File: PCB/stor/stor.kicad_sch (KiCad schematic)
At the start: 32 parts, among them J1 Conn_01x04_Socket, SW1 TS1603-TZ38HBM, SW2 TS1603-TZ38HBM, U1 STM32H723VGT6, U2 TYPE-C 24P-GTJB 040, U3 USB3300-EZK-TR, U4 TPS62177DQCR, X1 25mhz, X2 32.768k

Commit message: fill out usb phy
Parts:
- added R5: 12k, easyeda2kicad:R0402, symbol easyeda2kicad:RC0402FR-0712KL
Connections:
- net D+: now also U3.7 (DP)
- net D-: now also U3.8 (DM)
- net GND: now also Card1.10 (GND), Card1.11 (GND), Card1.12 (GND), Card1.13 (GND), Card1.6 (VSS), U3.1 (GND), U3.2 (GND), U3.33 (EPAD), R5.1
- net VBUS: now also U3.4 (VBUS)
- net VDD: now also Card1.4 (VDD), U3.16 (VDD3.3), U3.25 (VDD3.3), U3.30 (VDD3.3), U3.6 (VDD3.3)
- net PC0: now reaches U1.15 (PC0)
- net PC0: now also U3.13 (STP)
- net PC2: now reaches U1.17 (PC2_C)
- net PC2: now also U3.12 (DIR)
- net PC3: now reaches U1.18 (PC3_C)
- net PC3: now also U3.11 (NXT)
- net PA3: now reaches U1.25 (PA3)
- net PA3: now also U3.24 (DATA0)
- net PA5: now reaches U1.29 (PA5)
- net PA5: now also U3.14 (CLKOUT)
- net PB0: now reaches U1.34 (PB0)
- net PB0: now also U3.23 (DATA1)
- net PB1: now reaches U1.35 (PB1)
- net PB1: now also U3.22 (DATA2)
- net PB10: now reaches U1.46 (PB10)
- net PB10: now also U3.21 (DATA3)
- net PB11: now reaches U1.47 (PB11)
- net PB11: now also U3.20 (DATA4)
- net PB12: now reaches U1.51 (PB12)
- net PB12: now also U3.19 (DATA5)
- net PB13: now reaches U1.52 (PB13)
- net PB13: now also U3.18 (DATA6)
- net PC8: now reaches U1.65 (PC8)
- net PC8: now also Card1.7 (DAT0(D0))
- net PC9: now reaches U1.66 (PC9)
- net PC9: now also Card1.8 (DAT1(RSV))
- net PC10: now reaches U1.78 (PC10)
- net PC10: now also Card1.1 (DAT2(RSV))
- net PC11: now reaches U1.79 (PC11)
- net PC11: now also Card1.2 (CDDAT3(CS))
- net PD2: now reaches U1.83 (PD2)
- net PD2: now also Card1.3 (CMD(DI))
- net PB5: now reaches U1.91 (PB5)
- net PB5: now also U3.17 (DATA7)
- net at U3.32 (RBIAS): now also R5.2
- net PC12: now reaches Card1.5 (CLK(SCLK))
- no-connect marks 11 -> 14
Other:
- note added: "SD"
- note added: "TODO Card detect pin"
- note added: "TODO put a crystal here"
- note added: "USB PHY"
- note added: "to a GPIO"

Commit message: usb phy
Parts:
- added C18, C20, C22: 4.7uF, easyeda2kicad:C0402, symbol easyeda2kicad:CL05A475KP5NRNC
- added C19, C21, C23: 100nF, easyeda2kicad:C0402, symbol easyeda2kicad:CC0402KRX7R7BB104
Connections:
- net GND: now also C18.1, C19.1, C20.1, C21.1, C22.1, C23.1
- net at U3.15 (VDD1.8): now also C18.2, C19.2
- net at U3.26 (VDD1.8): now also C20.2, C21.2
- net XO: now reaches U3.27 (XO)
- net XI: now reaches U3.28 (XI)
- net at U3.29 (VDDA1.8): now also C22.2, C23.2
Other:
- moved on the sheet: Card1, R5, U3

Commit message: usb phy p much done and dusted
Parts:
- added C24, C25: 33pF, easyeda2kicad:C0402, symbol easyeda2kicad:CL05C330JB5NNNC
- added R6: 1mΩ, easyeda2kicad:R0402, symbol easyeda2kicad:RC0402FR-071ML
- added X3: 24mhz, easyeda2kicad:CRYSTAL-SMD_4P-L3.2-W2.5-BL, symbol easyeda2kicad:SX32Y024000BC1T001
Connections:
- net GND: now also C24.1, C25.1, X3.2 (GND), X3.4 (GND)
- net XI: now also C25.2, R6.2, X3.3
- net XO: now also C24.2, R6.1, X3.1
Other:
- moved on the sheet: C20, C21

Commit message: Update stor.kicad_sch
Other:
- note added: "TODO add esd protection"
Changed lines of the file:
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@@
+		)
+	)
+	(text "TODO add esd protection"
+		(exclude_from_sim no)
+		(at 130.302 224.282 0)
+		(effects
+			(font
+				(size 1.27 1.27)
+			)
 		)
 	)

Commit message: Update stor.kicad_sch
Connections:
- net VDD: now also U3.31 (REG_EN)
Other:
- note removed: "TODO put a crystal here"
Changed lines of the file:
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@@
 		)
 	)
-	(text "TODO put a crystal here"
-		(exclude_from_sim no)
-		(at 229.87 18.034 0)
+	(text "TODO Card detect pin"
+		(exclude_from_sim no)
+		(at 331.216 50.292 0)
 		(effects
 			(font
@@
 		)
 	)
-	(text "TODO Card detect pin"
-		(exclude_from_sim no)
-		(at 331.216 50.292 0)
+	(text "SD"
+		(exclude_from_sim no)
+		(at 275.844 16.51 0)
+		(effects
+			(font
+				(size 2.54 2.54)
+			)
+		)
+	)
+	(text "TODO add esd protection"
+		(exclude_from_sim no)
+		(at 130.302 224.282 0)
 		(effects
 			(font
@@
 		)
 	)
-	(text "SD"
-		(exclude_from_sim no)
-		(at 275.844 16.51 0)
+	(text "USBC"
+		(exclude_from_sim no)
+		(at 121.92 173.99 0)
 		(effects
 			(font
@@
 		)
 	)
-	(text "TODO add esd protection"
-		(exclude_from_sim no)
-		(at 130.302 224.282 0)
+	(text "STM and friends\n"
+		(exclude_from_sim no)
+		(at 32.512 154.178 0)
+		(effects
+			(font
+				(size 2.54 2.54)
+			)
+		)
+	)
+	(text "to a GPIO"
+		(exclude_from_sim no)
+		(at 218.44 113.03 90)
 		(effects
 			(font
@@
 		)
 	)
-	(text "USBC"
-		(exclude_from_sim no)
-		(at 121.92 173.99 0)
+	(text "USB PHY"
+		(exclude_from_sim no)
+		(at 202.692 21.082 0)
 		(effects
 			(font
@@
 		)
 	)
-	(text "STM and friends\n"
-		(exclude_from_sim no)
-		(at 32.512 154.178 0)
+	(text "Power"
+		(exclude_from_sim no)
+		(at 27.178 175.514 0)
 		(effects
 			(font
@@
 		)
 	)
-	(text "to a GPIO"
-		(exclude_from_sim no)
-		(at 218.44 113.03 90)
+	(text "??"
+		(exclude_from_sim no)
+		(at 25.908 45.974 0)
 		(effects
 			(font
@@
 		)
 	)
-	(text "USB PHY"
-		(exclude_from_sim no)
-		(at 202.692 21.082 0)
-		(effects
-			(font
-				(size 2.54 2.54)
-			)
-		)
-	)
-	(text "Power"
-		(exclude_from_sim no)
-		(at 27.178 175.514 0)
-		(effects
-			(font
-				(size 2.54 2.54)
-			)
-		)
-	)
-	(text "??"
-		(exclude_from_sim no)
-		(at 25.908 45.974 0)
+	(text "button, cap"
+		(exclude_from_sim no)
+		(at 27.178 24.892 0)
 		(effects
 			(font
@@
 		)
 	)
-	(text "button, cap"
-		(exclude_from_sim no)
-		(at 27.178 24.892 0)
-		(effects
-			(font
-				(size 1.27 1.27)
-			)
-		)
-	)
 	(junction
 		(at 264.16 54.61)
@@
 		)
 		(stroke
+			(width 0)
+			(type default)
+		)
+	)
+	(wire
+		(pts
+			(xy 220.98 53.34) (xy 223.52 53.34)
+		)
+		(stroke

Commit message: esd protection
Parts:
- added D2: PESD15VL2BT,215, easyeda2kicad:SOT-23-3_L2.9-W1.3-P1.90-LS2.4-BR, symbol easyeda2kicad:PESD15VL2BT,215
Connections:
- net D+: now also D2.2
- net D-: now also D2.1
- net GND: now also D2.3
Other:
- note added: "TODO to a GPIO"
- note removed: "TODO add esd protection"
- note removed: "to a GPIO"
- moved on the sheet: R2, R3, U2

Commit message: schematic is, as far as I know, done!
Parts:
- added C26: 100nF, easyeda2kicad:C0402, symbol easyeda2kicad:CC0402KRX7R7BB104
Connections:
- net VREF is gone; now on net VDD: U1.20 (VREF+)
- net GND: now also C26.1
- net VDD: now also C26.2
- net PD3: now reaches U1.84 (PD3)
- net PD3: now also U3.9 (RESET)
- net PD4: now reaches U1.85 (PD4)
- net PD4: now also Card1.9 (CD)
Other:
- note added: "can be any gpio"
- note removed: "??"
- note removed: "TODO Card detect pin"
- note removed: "TODO to a GPIO"
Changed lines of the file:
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@@
 		)
 	)
-	(text "TODO Card detect pin"
+	(text "can be any gpio\n"
 		(exclude_from_sim no)
-		(at 331.216 50.292 0)
+		(at 330.708 44.704 0)
 		(effects
 			(font
@@
 		)
 	)
-	(text "TODO to a GPIO"
+	(text "can be any gpio"
 		(exclude_from_sim no)
-		(at 218.44 116.078 90)
+		(at 215.646 114.3 90)
 		(effects
 			(font
@@
 		)
 	)
-	(text "??"
-		(exclude_from_sim no)
-		(at 25.908 45.974 0)
-		(effects
-			(font
-				(size 1.27 1.27)
-			)
-		)
-	)
 	(text "button, cap"
 		(exclude_from_sim no)
@@
 	)
 	(junction
+		(at 93.98 116.84)
+		(diameter 0)
+		(color 0 0 0 0)
+	)
+	(junction
 		(at 64.77 48.26)
 		(diameter 0)
@@
 	)
 	(junction
+		(at 93.98 106.68)
+		(diameter 0)
+		(color 0 0 0 0)
+	)
+	(junction
 		(at 63.5 106.68)
 		(diameter 0)
@@
 	(wire
 		(pts
+			(xy 93.98 106.68) (xy 99.06 106.68)
+		)
+		(stroke
+			(width 0)
+			(type default)
+		)
+	)
+	(wire
+		(pts
 			(xy 251.46 19.05) (xy 256.54 19.05)
 		)
@@
 	(wire
 		(pts
+			(xy 109.22 71.12) (xy 116.84 71.12)
+		)
+		(stroke
+			(width 0)
+			(type default)
+		)
+	)
+	(wire
+		(pts
 			(xy 97.79 189.23) (xy 100.33 189.23)
 		)
@@
 	(wire
 		(pts
+			(xy 93.98 116.84) (xy 99.06 116.84)
+		)
+		(stroke
+			(width 0)
+			(type default)
+		)
+	)
+	(wire
+		(pts
 			(xy 80.01 17.78) (xy 80.01 19.05)
 		)
@@
 		)
 	)
+	(label "PD3"
+		(at 157.48 63.5 0)
+		(effects
+			(font
+				(size 1.27 1.27)
+			)
+			(justify left bottom)
+		)
+	)
 	(label "PD2"
 		(at 288.29 50.8 180)
@@
 		)
 	)
+	(label "PD4"
+		(at 157.48 60.96 0)
+		(effects
+			(font
+				(size 1.27 1.27)
+			)
+			(justify left bottom)
+		)
+	)
 	(label "PC0"
 		(at 228.6 106.68 270)
@@
 		)
 	)
+	(label "PD3"
+		(at 218.44 106.68 270)
+		(effects
+			(font
+				(size 1.27 1.27)
+			)
+			(justify right bottom)
+		)
+	)
 	(label "PC15"
 		(at 116.84 43.18 180)
@@
 		)
 	)
+	(label "PD4"
+		(at 326.39 48.26 0)
+		(effects
+			(font
+				(size 1.27 1.27)
+			)
+			(justify left bottom)
+		)
+	)
 	(label "PA5"
 		(at 116.84 93.98 180)
@@
 		)
 	)
+	(label "VDD"
+		(at 109.22 71.12 180)
+		(effects
+			(font
+				(size 1.27 1.27)
+			)
+			(justify right bottom)
+		)
+	)
 	(label "VBUS"
 		(at 147.32 205.74 180)
@@
 		)
 	)
-	(global_label "VREF"
-		(shape input)
-		(at 116.84 71.12 180)
-		(fields_autoplaced yes)
-		(effects
-			(font
-				(size 1.27 1.27)
-			)
-			(justify right)
-		)
-		(property "Intersheetrefs" "${INTERSHEET_REFS}"
-			(at 109.2586 71.12 0)
-			(hide yes)
-			(show_name no)
-			(do_not_autoplace no)
-			(effects
-				(font
-					(size 1.27 1.27)
-				)
-				(justify right)
-			)
-		)
-	)
-	(global_label "VREF"
-		(shape input)
-		(at 29.21 43.18 180)
-		(fields_autoplaced yes)
-		(effects
-			(font
-				(size 1.27 1.27)
-			)
-			(justify right)
-		)
-		(property "Intersheetrefs" "${INTERSHEET_REFS}"
-			(at 21.6286 43.18 0)
-			(hide yes)
-			(show_name no)
-			(do_not_autoplace no)
-			(effects
-				(font
-					(size 1.27 1.27)
-				)
-				(justify right)
-			)
-		)
-	)
 	(symbol
 		(lib_id "easyeda2kicad:RC0402FR-071ML")
@@
 					(unit 1)
 				)
+			)
+		)
+	)
+	(symbol
+		(lib_id "easyeda2kicad:CC0402KRX7R7BB104")
+		(at 99.06 111.76 90)
+		(unit 1)
+		(body_style 1)
+		(exclude_from_sim no)
+		(in_bom yes)
+		(on_board yes)
+		(in_pos_files yes)
+		(dnp no)
+		(fields_autoplaced yes)
+		(property "Reference" "C26"
+			(at 102.87 110.4899 90)
+			(show_name no)
+			(do_not_autoplace no)
+			(effects
+				(font
+					(size 1.27 1.27)
+				)
+				(justify right)
+			)
+		)
+		(property "Value" "100nF"
+			(at 102.87 113.0299 90)
+			(show_name no)
+			(do_not_autoplace no)
+			(effects
+				(font
+					(size 1.27 1.27)
+				)
+				(justify right)
+			)
+		)
+		(property "Footprint" "easyeda2kicad:C0402"
+			(at 106.68 111.76 0)
+			(hide yes)
+			(show_name no)
+			(do_not_autoplace no)
+			(effects
+				(font
+					(size 1.27 1.27)
+				)
+			)
+		)
+		(property "Datasheet" "https://lcsc.com/product-detail/Multilayer-Ceramic-Capacitors-MLCC-SMD-SMT_100nF-104-10-16V_C60474.html"
+			(at 109.22 111.76 0)
+			(hide yes)
+			(show_name no)
+			(do_not_autoplace no)
+			(effects
+				(font
+					(size 1.27 1.27)
+				)
+			)
+		)
+		(property "Description" ""
+			(at 99.06 111.76 0)
+			(hide yes)
+			(show_name no)
+			(do_not_autoplace no)
+			(effects
+				(font
+					(size 1.27 1.27)
+				)
+			)
+		)
+		(property "Manufacturer" "YAGEO(国巨)"
+			(at 111.76 111.76 0)
+			(hide yes)
+			(show_name no)
+			(do_not_autoplace no)
+			(effects
+				(font
+					(size 1.27 1.27)
+				)
+			)
+		)
+		(property "MPN" "CC0402KRX7R7BB104"
+			(at 114.3 111.76 0)
+			(hide yes)
+			(show_name no)
+			(do_not_autoplace no)
+			(effects
+				(font
+					(size 1.27 1.27)
+				)
+			)
+		)
+		(property "LCSC Part" "C60474"
+			(at 116.84 111.76 0)
+			(hide yes)
+			(show_name no)
+			(do_not_autoplace no)
+			(effects
+				(font
+					(size 1.27 1.27)
+				)
+			)
+		)
+		(pin "2"
+		)
+		(pin "1"
+		)
+		(instances
+			(project "stor"
+				(path "/d0bb07ec-2650-48b2-bcd0-488070624271"
+					(reference "C26")
+					(unit 1)
+				)

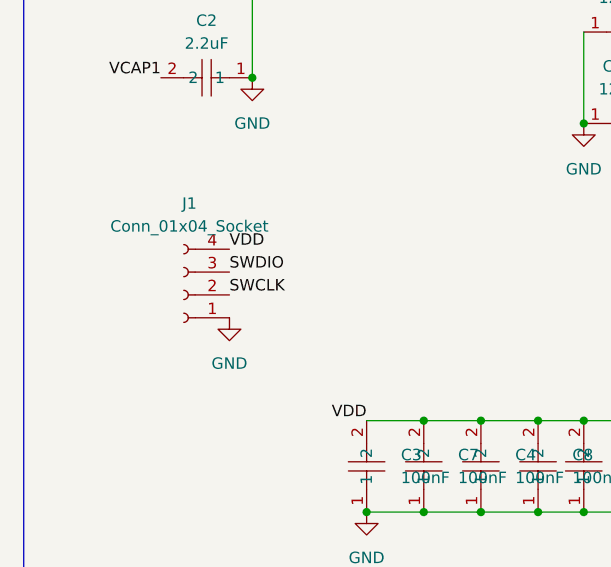
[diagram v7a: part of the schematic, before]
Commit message: placement for all but the silly caps
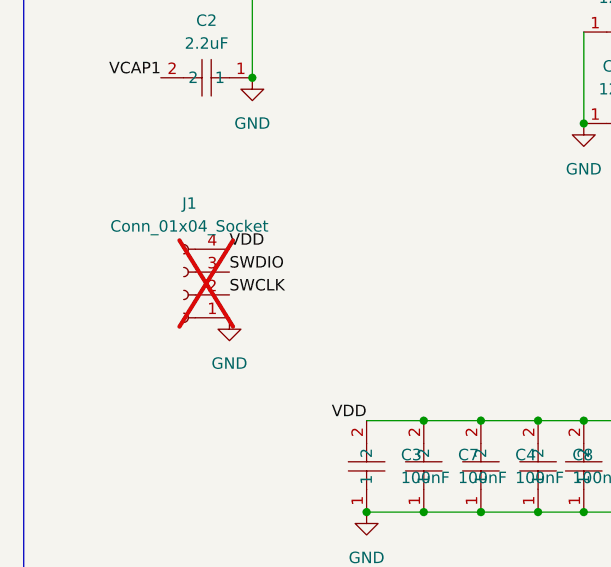
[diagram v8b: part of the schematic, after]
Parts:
- J1: footprint (none) -> Connector_PinHeader_2.54mm:PinHeader_1x04_P2.54mm_Vertical; now not fitted
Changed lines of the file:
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@@
 		(on_board yes)
 		(in_pos_files yes)
-		(dnp no)
+		(dnp yes)
 		(fields_autoplaced yes)
 		(property "Reference" "J1"
@@
 			)
 		)
-		(property "Footprint" ""
+		(property "Footprint" "Connector_PinHeader_2.54mm:PinHeader_1x04_P2.54mm_Vertical"
 			(at 30.48 92.71 0)
 			(hide yes)
